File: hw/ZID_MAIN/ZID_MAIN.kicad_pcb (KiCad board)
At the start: 2 copper layers, 213 parts, among them J1 Conn 1x04 0.1" Socket, J10 FFC/FPC-40 Socket, J11 JST-PH-K B6B, J14 USB-C PWR ONLY, J2 JST-PH-K B6B, J3 Conn 1x02 0.1" pin, J4 Conn 1x03 0.1" pin, J5 Conn 1x08 0.1" pin, J6 Conn 1x08 0.1" pin, J7 Conn 2x04 0.1" pin, J8 Conn 2x02 0.1" pin, J9 Conn 2x04 0.1" pin, M1 WS-RP2040-Zero, SW1 SW_Push, SW2 SW_DIP_x02, U1 OSC-20MHz, U10 74LVC2G04, U11 74LVC125AS, U12 74LVC273, U13 74FCT2245, U14 AS7C1024B, U15 74FCT2245, U16 74FCT2245, U17 74FCT2245, U18 ATF1508AS, U19 74HCT166, U2 74FCT2245, U20 74FCT2244, U21 74HCT166, U22 ATF1504AS-44T, U23 74AHCT00, U24 74FCT2244, U25 ATF1504AS-44T, U26 ATF1504AS-44T, U27 ATF1504AS-44T, U28 ATF1504AS-44T, U3 24LC32, U4 MIC2775, U5 SST39SF010, U6 74LVC245, U7 74FCT2245, U8 74AHCT14, U9 Z80 C20MHz-PLCC

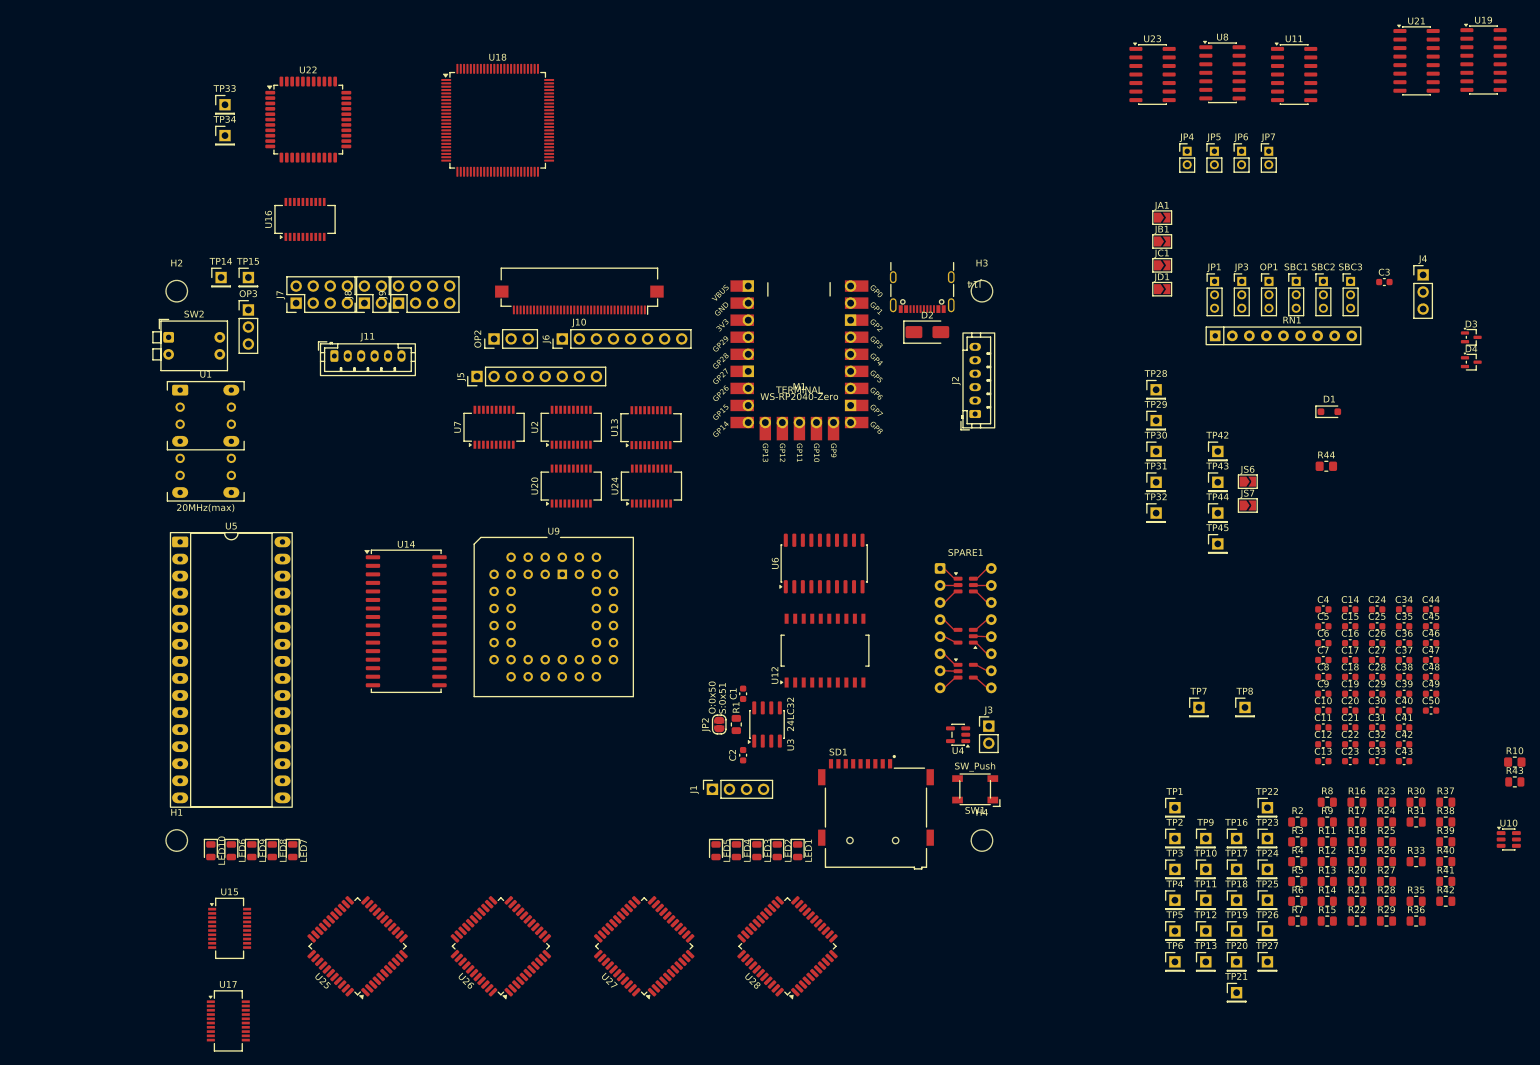
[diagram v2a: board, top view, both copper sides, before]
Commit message: PCB: All components placed V0.1
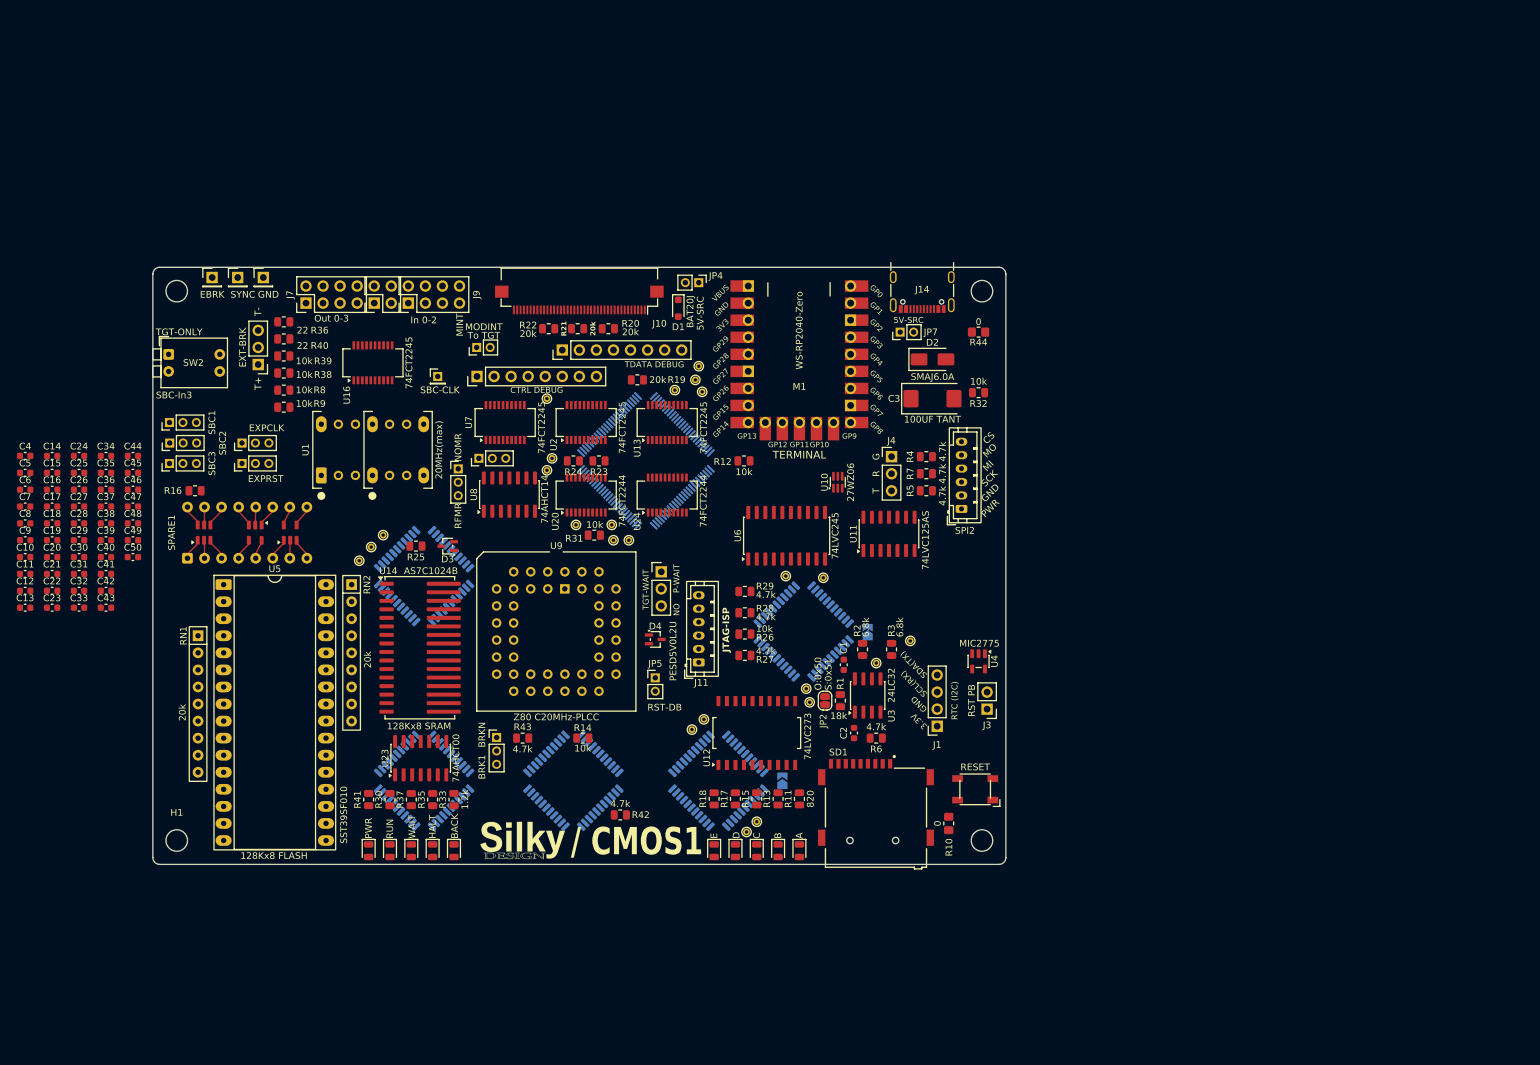
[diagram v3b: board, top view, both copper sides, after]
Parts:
- removed JA1, JB1, JS6, JS7: SolderJumper_2_Open, Jumper:SolderJumper-2_P1.3mm_Open_TrianglePad1.0x1.5mm
- removed TP19, TP20, TP23, TP24, TP27, TP30, TP42, TP43, TP44, TP45: TestPoint, Connector_PinHeader_2.54mm:PinHeader_1x01_P2.54mm_Vertical
- removed U15, U17: 74FCT2245, Package_SO:SSOP-20_3.9x8.7mm_P0.635mm
- removed U19, U21: 74HCT166, Package_SO:SOIC-16_3.9x9.9mm_P1.27mm
- added G***: LOGO, AES_Library:SILKY-DESIGN-logo-0_50-AES, F.Cu at (113.9, 141.2)
- added OP4: AES-Option_A-B_2mm, Connector_PinHeader_2.00mm:PinHeader_1x03_P2.00mm_Vertical, F.Cu at (109.9, 125.9)
- added R32: 10k, Resistor_SMD:R_0805_2012Metric, F.Cu at (181.7, 74.5)
- added RN2: 20k, Resistor_THT:R_Array_SIP9, F.Cu at (88.3, 103.1)
- added SPRU8F1: Conn_01x03_Pin, Connector_PinHeader_2.00mm:PinHeader_1x03_P2.00mm_Vertical, F.Cu at (107.3, 84.3)
- C3: value 100uF -> 100UF TANT; footprint Capacitor_SMD:C_0603_1608Metric -> Capacitor_Tantalum_SMD:CP_EIA-7343-31_Kemet-D_HandSolder
- JC1, JD1, U18, U22, U25, U26, U27, U28: moved to B.Cu
- TP1: footprint Connector_PinHeader_2.54mm:PinHeader_1x01_P2.54mm_Vertical -> Connector_PinHeader_2.00mm:PinHeader_1x01_P2.00mm_Vertical
- TP10, TP11, TP12, TP13, TP17, TP18, TP2, TP21, TP22, TP25, TP26, TP28, TP29, TP3, TP31, TP32, TP33, TP34, TP4, TP5, TP6, TP7, TP8, TP9: footprint Connector_PinHeader_2.54mm:PinHeader_1x01_P2.54mm_Vertical -> TestPoint:TestPoint_THTPad_D1.0mm_Drill0.5mm
- TP16: value TestPoint -> GND-CONN
- U1: footprint AES_Library:OSC-8_14-AES -> AES_Library:OSC-8_14-CO-AES
- U10: value 74LVC2G04 -> 27WZ06; footprint Package_TO_SOT_SMD:SOT-23-6 -> Package_TO_SOT_SMD:SOT-363_SC-70-6
- U14: footprint Package_SO:SOJ-32_10.16x20.955mm_P1.27mm -> AES_Library:SOJ-32_WN-AES
- moved C24 194.6 mm to (47.7, 84.0)
- moved C25 194.6 mm to (47.7, 86.5)
- moved C26 194.6 mm to (47.7, 89.0)
- moved C27 194.6 mm to (47.7, 91.5)
- moved C28 194.6 mm to (47.7, 94.0)
- moved C29 194.6 mm to (47.7, 96.5)
- moved C30 194.6 mm to (47.7, 99.0)
- moved C31 194.6 mm to (47.7, 101.5)
- moved C32 194.6 mm to (47.7, 104.0)
- moved C33 194.6 mm to (47.7, 106.6)
- moved C10 194.6 mm to (39.7, 99.0)
- moved C11 194.6 mm to (39.7, 101.5)
- moved C12 194.6 mm to (39.7, 104.0)
- moved C13 194.6 mm to (39.7, 106.6)
- moved C14 194.6 mm to (43.7, 84.0)
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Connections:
- RN1 pad 2: /ZA12 -> /ZA7
- RN1 pad 3: /ZA11 -> /ZA6
- RN1 pad 4: /ZA10 -> /ZA5
- RN1 pad 5: /ZA9 -> /ZA4
- RN1 pad 6: /ZA13 -> /ZA3
- RN1 pad 7: /ZA8 -> /ZA2
- RN1 pad 8: /ZA14 -> /ZA1
- RN1 pad 9: /ZA15 -> /ZA0
- TP28 pad 1: /GPO_B- -> /GPO_C-
- TP29 pad 1: /GPO_B- -> /GPO_D-
- TP31 pad 1: /GPI_B- -> /GPI_C-
- TP32 pad 1: /GPI_B- -> /GPI_D-
- U1 pad 11: /_CLK -> +5V
- U1 pad 4: GND -> +5V
- U10 pad 6: /MINT- -> /MODINT-
- U2 pad 19: /ZRST- -> /ZRST
- U25 pad 10: /IO10A -> /ZA9
- U25 pad 11: /LA0 -> /ZA7
- U25 pad 12: /LA1 -> /ZA0
- U25 pad 13: /LA2 -> /ZA11
- U25 pad 14: /LA3 -> /ZA15
- U25 pad 15: /LA4 -> /ZA14
- U25 pad 18: /LA5 -> /ZA8
- U25 pad 19: /LA6 -> /PC_LATCH-
- U25 pad 2: /ENBL_DOA -> /ZA10
- U25 pad 20: /LA7 -> /ZA6
- U25 pad 21: /LA8 -> /ZA5
- U25 pad 22: /LA9 -> /ZA4
- U25 pad 23: /LA10 -> /ZA3
- U25 pad 25: /LA11 -> /BRK1_AEQ-
- U25 pad 27: /LA12 -> /ZA2
- U25 pad 28: /LA13 -> /ZA1
- U25 pad 3: /ADDR_DOA -> /BA_CLR-
- U25 pad 30: /LA14 -> /ZD7
- U25 pad 31: /LA15 -> GND
- U25 pad 33: /MINT- -> /SD_OUTIN
- U25 pad 34: /MODINT- -> Net-(OP4-C)
- U25 pad 35: /BA_CLR- -> /BA_CLK
- U25 pad 37: /BA_CLK -> /BRKPC_RD-
- U25 pad 42: /BRKN_AEQ- -> /ADDR_DOA
- U25 pad 43: /BRK1_AEQ- -> /ZA13
- U25 pad 44: /BRKHWDET- -> /ZA12
- U25 pad 6: /ZD7 -> /BRKHWDET-
- U25 pad 8: /IO8A -> /ENBL_DOA
- U26 pad 10: /IO10B -> /ZA13
- U26 pad 11: /LA0 -> /ZA12
- U26 pad 12: /LA1 -> /PC_LATCH-
- U26 pad 13: /LA2 -> /ZA4
- U26 pad 14: /LA3 -> /ZA5
- U26 pad 15: /LA4 -> /ZA6
- U26 pad 18: /LA5 -> /ZA14
- U26 pad 19: /LA6 -> /ZA15
- U26 pad 2: /ENBL_DOB -> /ZA0
- U26 pad 20: /LA7 -> /ZA11
- U26 pad 21: /LA8 -> /ZA9
- U26 pad 22: /LA9 -> /ZA8
- U26 pad 23: /LA10 -> /ZA2
- U26 pad 25: /LA11 -> /BRKN_AEQ-
- U26 pad 27: /LA12 -> /ZA1
- U26 pad 28: /LA13 -> /ZA3
- U26 pad 3: /ADDR_DOB -> /BA_CLR-
- U26 pad 30: /LA14 -> /SD_OUTIN
- U26 pad 31: /LA15 -> /ADDR_DOA
- U26 pad 33: /GPI_A- -> /PCRD_DIN
- U26 pad 34: /GPO_A- -> /BRKN_AEQ-
- U26 pad 35: /BA_CLR- -> /BA_CLK
- U26 pad 37: /BA_CLK -> /BRKPC_RD-
- U26 pad 42: /BRKN_AEQ- -> /ADDR_DOB
- U26 pad 43: /BRKN_AEQ- -> /ZA10
- U26 pad 44: /BRKHWDET- -> /ZA7
- U26 pad 6: /ADDR_DOA -> /BRKHWDET-
- U26 pad 8: /IO8B -> /ENBL_DOB
- U27 pad 11: /LA0 -> /ZA0
- U27 pad 12: /LA1 -> /ZA1
- U27 pad 13: /LA2 -> /ZA2
- U27 pad 14: /LA3 -> /ZA3
- U27 pad 15: /LA4 -> /ZA4
- U27 pad 18: /LA5 -> /ZA5
- U27 pad 19: /LA6 -> /ZA6
- U27 pad 20: /LA7 -> /ZA7
- U27 pad 21: /LA8 -> /ZA8
- U27 pad 22: /LA9 -> /ZA9
- U27 pad 23: /LA10 -> /ZA10
- U27 pad 25: /LA11 -> /ZA11
- U27 pad 27: /LA12 -> /ZA12
- U27 pad 28: /LA13 -> /ZA13
- U27 pad 30: /LA14 -> /ZA14
- U27 pad 31: /LA15 -> /ZA15
- U27 pad 33: /GPI_B- -> /GPI_C-
- U27 pad 34: /GPO_B- -> /GPO_C-
- U28 pad 11: /LA0 -> /ZA0
- U28 pad 12: /LA1 -> /ZA1
- U28 pad 13: /LA2 -> /ZA2
- U28 pad 14: /LA3 -> /ZA3
- U28 pad 15: /LA4 -> /ZA4
- U28 pad 18: /LA5 -> /ZA5
- U28 pad 19: /LA6 -> /ZA6
- U28 pad 20: /LA7 -> /ZA7
- U28 pad 21: /LA8 -> /ZA8
- U28 pad 22: /LA9 -> /ZA9
- U28 pad 23: /LA10 -> /ZA10
- U28 pad 25: /LA11 -> /ZA11
- U28 pad 27: /LA12 -> /ZA12
- U28 pad 28: /LA13 -> /ZA13
- U28 pad 30: /LA14 -> /ZA14
- U28 pad 31: /LA15 -> /ZA15
- U28 pad 33: /GPI_B- -> /GPI_D-
- U28 pad 34: /GPO_B- -> /GPO_D-
- U7 pad 19: /ZRST- -> /ZRST
- U8 pad 10: Net-(TP43-Pad1) -> /ZRST
- U8 pad 11: Net-(JS6-B) -> /ZRST-
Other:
- board outline added: 127 x 88.9 mm
- board text added: "/ CMOS1"
